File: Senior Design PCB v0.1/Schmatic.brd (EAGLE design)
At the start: 101.3 x 67.5 mm, 243 parts, among them IC1 TMC2208, IC2 TMC2208, IC3 TMC2208, IC4 TMC2208, IC5 TMC2208, IC6 CP2104, Q1 mmbt2222, Q2 mmbt2222, Q3 MMBT4403, Q4 AOD417, Q5 MMBT4403, Q6 MMBT4403, Q7 DMG3415U, U1 PCA9685, U2 AP2112-3.3, U3 HTU21DF, U4 HX711, U5 HX711, U6 HX711, U7 SX1509, X2 ESP32_WROOM32_SKINNY

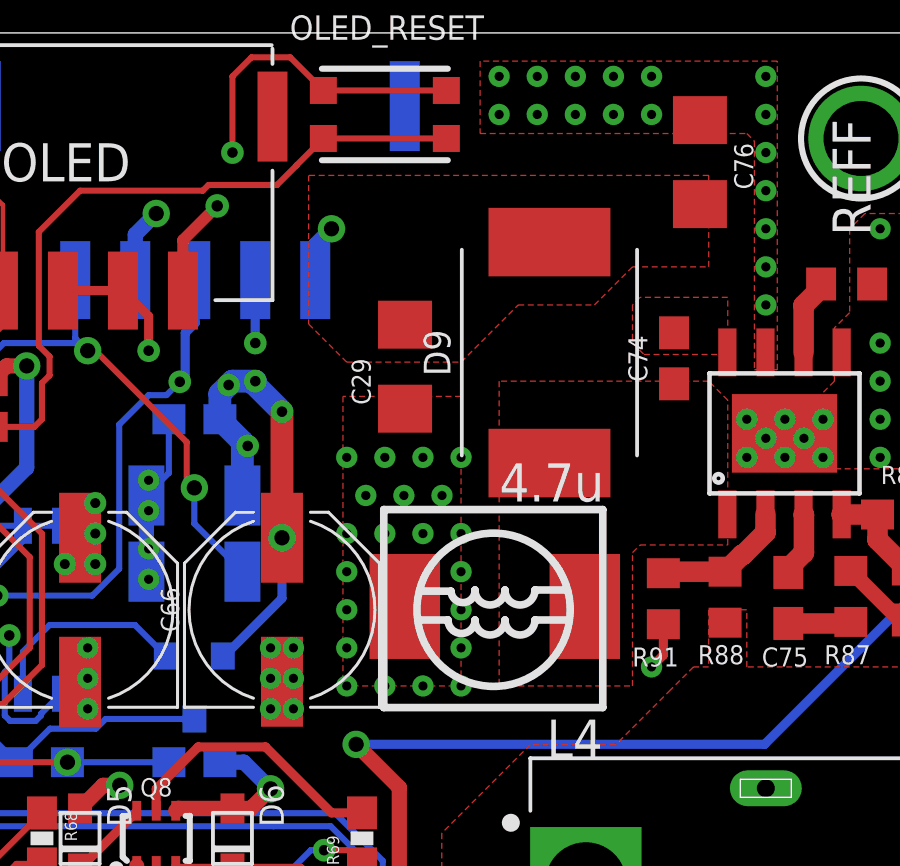
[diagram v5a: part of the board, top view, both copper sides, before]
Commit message: added vias for ground planes on buck
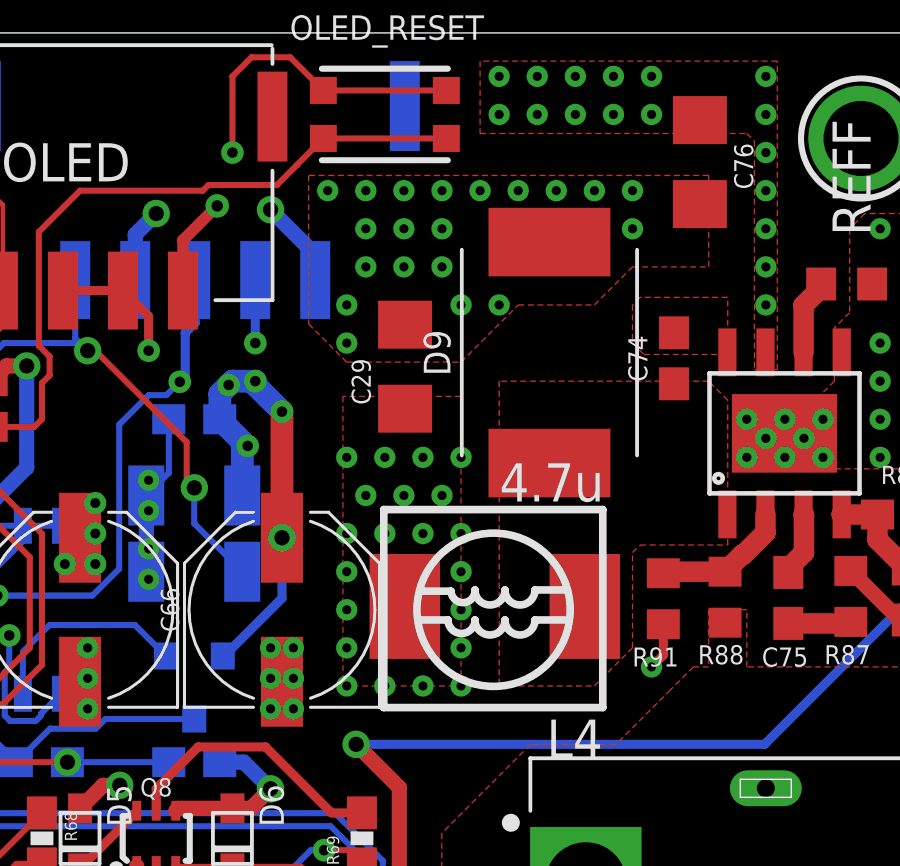
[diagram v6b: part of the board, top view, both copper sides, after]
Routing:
- net GND: track 460.8 -> 461.9 mm, vias 208 -> 228
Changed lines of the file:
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@@
 <drawing>
 <settings>
-<setting alwaysvectorfont="yes"/>
+<setting alwaysvectorfont="no"/>
 <setting verticaltext="up"/>
 </settings>
@@
 <wire x1="57.37" y1="59.402" x2="58.039" y2="60.071" width="0.508" layer="16"/>
 <via x="58.039" y="60.071" extent="1-16" drill="0.508"/>
-<wire x1="72.61" y1="57.98" x2="72.61" y2="59.148" width="0.508" layer="16"/>
-<wire x1="72.61" y1="59.148" x2="73.152" y2="59.69" width="0.508" layer="16"/>
-<via x="73.152" y="59.69" extent="1-16" drill="0.508"/>
+<wire x1="72.61" y1="57.98" x2="72.61" y2="58.835" width="0.508" layer="16"/>
+<wire x1="72.61" y1="58.835" x2="71.12" y2="60.325" width="0.508" layer="16"/>
+<via x="71.12" y="60.325" extent="1-16" drill="0.508"/>
 <wire x1="66.61" y1="59.498" x2="66.61" y2="57.98" width="0.508" layer="16"/>
 <wire x1="66.61" y1="59.498" x2="67.31" y2="60.198" width="0.508" layer="16"/>
@@
 <wire x1="93.687" y1="46.648" x2="93.98" y2="46.355" width="0.508" layer="1"/>
 <via x="93.98" y="46.355" extent="1-16" drill="0.508"/>
+<via x="73.025" y="60.96" extent="1-16" drill="0.3048"/>
+<via x="74.295" y="60.96" extent="1-16" drill="0.3048"/>
+<via x="75.565" y="60.96" extent="1-16" drill="0.3048"/>
+<via x="76.835" y="60.96" extent="1-16" drill="0.3048"/>
+<via x="76.835" y="59.69" extent="1-16" drill="0.3048"/>
+<via x="75.565" y="59.69" extent="1-16" drill="0.3048"/>
+<via x="74.295" y="59.69" extent="1-16" drill="0.3048"/>
+<via x="74.295" y="58.42" extent="1-16" drill="0.3048"/>
+<via x="75.565" y="58.42" extent="1-16" drill="0.3048"/>
+<via x="76.835" y="58.42" extent="1-16" drill="0.3048"/>
+<via x="77.47" y="57.15" extent="1-16" drill="0.3048"/>
+<via x="78.74" y="57.15" extent="1-16" drill="0.3048"/>
+<via x="73.66" y="55.88" extent="1-16" drill="0.3048"/>
+<via x="73.66" y="57.15" extent="1-16" drill="0.3048"/>
+<via x="78.105" y="60.96" extent="1-16" drill="0.3048"/>
+<via x="79.375" y="60.96" extent="1-16" drill="0.3048"/>
+<via x="80.645" y="60.96" extent="1-16" drill="0.3048"/>
+<via x="81.915" y="60.96" extent="1-16" drill="0.3048"/>
+<via x="83.185" y="60.96" extent="1-16" drill="0.3048"/>
+<via x="83.185" y="59.69" extent="1-16" drill="0.3048"/>
 <wire x1="71.12" y1="44.704" x2="71.501" y2="44.59" width="0" layer="19" extent="1-1"/>
 <wire x1="81.026" y1="18.542" x2="81.02091875" y2="18.56231875" width="0" layer="19" extent="1-1"/>
@@
 <vertex x="75.676759375" y="40.370759375"/>
 <vertex x="79.629" y="44.323"/>
-<vertex x="79.629" y="59.182"/>
-<vertex x="72.39" y="59.182"/>
-<vertex x="72.39" y="51.90460625"/>
+<vertex x="79.629" y="53.086"/>
+<vertex x="78.359" y="54.356"/>
+<vertex x="73.406" y="54.356"/>
+<vertex x="72.263" y="53.213"/>
+<vertex x="72.263" y="51.77749375"/>
 <vertex x="61.356240625" y="40.861134375"/>
 <vertex x="61.356240625" y="36.45408125"/>
@@
 <vertex x="78.74" y="54.61"/>
 <vertex x="78.74" y="44.45"/>
-<vertex x="83.185" y="44.45"/>
+<vertex x="81.915" y="44.45"/>
+<vertex x="83.185" y="45.72"/>
 <vertex x="83.185" y="48.895"/>
 <vertex x="83.439" y="49.149"/>
